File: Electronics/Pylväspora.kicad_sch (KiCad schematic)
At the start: 19 parts, among them SW1 SW_Push, SW2 SW_Push, U1 ATtiny814-SS, U2 AMS1117-3.3

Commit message: Corrected jst model footprints
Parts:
- Feedback1: footprint Connector_PinSocket_2.54mm:PinSocket_1x03_P2.54mm_Vertical -> Connector_JST:JST_EH_B3B-EH-A_1x03_P2.50mm_Vertical
- PWM_out1: footprint Connector_PinSocket_2.54mm:PinSocket_1x01_P2.54mm_Vertical -> Connector_PinHeader_2.54mm:PinHeader_1x01_P2.54mm_Vertical
- PWR1: footprint Connector_PinSocket_2.54mm:PinSocket_1x02_P2.54mm_Vertical -> Connector_JST:JST_EH_B2B-EH-A_1x02_P2.50mm_Vertical
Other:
- note added: "Buttons"
- note added: "Drill Press controller"
- note added: "Mounting"
- note added: "POWER"
- moved on the sheet: C1, C2, C3, C4, H2, H3, H4, PWR1, SW1, SW2, U2

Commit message: Software ios, display driving logic, buttons
Software ios, display driving logic, buttons
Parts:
- C1: value C -> 100u
- C2: value C -> 10u
- C3, C4: value C -> 10n
- R1, R2: value R -> 1k
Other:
- note added: "3.2mm Drillsize"
- note added: "Outputs"
- moved on the sheet: R1, pinheader1
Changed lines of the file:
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@@
+		)
+	)
+	(rectangle
+		(start 181.61 29.21)
+		(end 251.46 74.93)
+		(stroke
+			(width 0)
+			(type default)
+		)
+		(fill
+			(type none)
 		)
 	)
@@
 		)
 	)
+	(text "3.2mm Drillsize"
+		(exclude_from_sim no)
+		(at 68.834 127.254 0)
+		(effects
+			(font
+				(size 1.27 1.27)
+			)
+		)
+	)
+	(text "Outputs"
+		(exclude_from_sim no)
+		(at 225.298 34.036 0)
+		(effects
+			(font
+				(size 1.27 1.27)
+			)
+		)
+	)
 	(junction
 		(at 224.79 119.38)
@@
 	(wire
 		(pts
+			(xy 205.74 59.69) (xy 209.55 59.69)
+		)
+		(stroke
+			(width 0)
+			(type default)
+		)
+	)
+	(wire
+		(pts
 			(xy 224.79 119.38) (xy 224.79 124.46)
 		)
@@
 	(wire
 		(pts
-			(xy 198.12 62.23) (xy 209.55 62.23)
+			(xy 203.2 62.23) (xy 209.55 62.23)
 		)
 		(stroke
@@
 	(wire
 		(pts
+			(xy 205.74 55.88) (xy 205.74 59.69)
+		)
+		(stroke
+			(width 0)
+			(type default)
+		)
+	)
+	(wire
+		(pts
 			(xy 201.93 106.68) (xy 209.55 106.68)
 		)
@@
 	(wire
 		(pts
+			(xy 203.2 46.99) (xy 207.01 46.99)
+		)
+		(stroke
+			(width 0)
+			(type default)
+		)
+	)
+	(wire
+		(pts
+			(xy 203.2 46.99) (xy 203.2 48.26)
+		)
+		(stroke
+			(width 0)
+			(type default)
+		)
+	)
+	(wire
+		(pts
 			(xy 43.18 31.75) (xy 43.18 34.29)
 		)
@@
 	(wire
 		(pts
-			(xy 177.8 35.56) (xy 180.34 35.56)
+			(xy 204.47 39.37) (xy 207.01 39.37)
 		)
 		(stroke
@@
 	(wire
 		(pts
-			(xy 179.07 40.64) (xy 180.34 40.64)
-		)
-		(stroke
-			(width 0)
-			(type default)
-		)
-	)
-	(wire
-		(pts
-			(xy 177.8 38.1) (xy 180.34 38.1)
+			(xy 205.74 44.45) (xy 207.01 44.45)
+		)
+		(stroke
+			(width 0)
+			(type default)
+		)
+	)
+	(wire
+		(pts
+			(xy 204.47 41.91) (xy 207.01 41.91)
 		)
 		(stroke
@@
 	(wire
 		(pts
+			(xy 195.58 62.23) (xy 194.31 62.23)
+		)
+		(stroke
+			(width 0)
+			(type default)
+		)
+	)
+	(wire
+		(pts
 			(xy 107.95 78.74) (xy 111.76 78.74)
 		)
@@
 	(wire
 		(pts
-			(xy 204.47 59.69) (xy 209.55 59.69)
+			(xy 209.55 55.88) (xy 205.74 55.88)
 		)
 		(stroke
@@
 	(global_label "3.3V"
 		(shape input)
-		(at 204.47 59.69 180)
+		(at 209.55 55.88 180)
 		(fields_autoplaced yes)
 		(effects
@@
 		)
 		(property "Intersheetrefs" "${INTERSHEET_REFS}"
-			(at 197.3724 59.69 0)
+			(at 202.4524 55.88 0)
 			(effects
 				(font
@@
 	(global_label "3.3V"
 		(shape input)
-		(at 179.07 40.64 180)
+		(at 205.74 44.45 180)
 		(fields_autoplaced yes)
 		(effects
@@
 		)
 		(property "Intersheetrefs" "${INTERSHEET_REFS}"
-			(at 171.9724 40.64 0)
+			(at 198.6424 44.45 0)
 			(effects
 				(font
@@
 	(global_label "SCK"
 		(shape input)
-		(at 177.8 35.56 180)
+		(at 204.47 39.37 180)
 		(fields_autoplaced yes)
 		(effects
@@
 		)
 		(property "Intersheetrefs" "${INTERSHEET_REFS}"
-			(at 171.0653 35.56 0)
+			(at 197.7353 39.37 0)
 			(effects
 				(font
@@
 	(global_label "SDA"
 		(shape input)
-		(at 177.8 38.1 180)
+		(at 204.47 41.91 180)
 		(fields_autoplaced yes)
 		(effects
@@
 		)
 		(property "Intersheetrefs" "${INTERSHEET_REFS}"
-			(at 171.2467 38.1 0)
+			(at 197.9167 41.91 0)
 			(effects
 				(font
@@
 	(global_label "PA4"
 		(shape input)
-		(at 190.5 62.23 180)
+		(at 194.31 62.23 180)
 		(fields_autoplaced yes)
 		(effects
@@
 		)
 		(property "Intersheetrefs" "${INTERSHEET_REFS}"
-			(at 183.9467 62.23 0)
+			(at 187.7567 62.23 0)
 			(effects
 				(font
@@
 			)
 		)
-		(property "Value" "C"
+		(property "Value" "10u"
 			(at 78.74 46.9899 0)
 			(effects
@@
 			)
 		)
-		(property "Value" "R"
+		(property "Value" "1k"
 			(at 152.4 72.39 90)
 			(effects
@@
 			)
 		)
-		(property "Value" "C"
+		(property "Value" "10n"
 			(at 241.3 116.8399 0)
 			(effects
@@
 			)
 		)
-		(property "Value" "C"
+		(property "Value" "100u"
 			(at 50.8 46.9899 0)
 			(effects
@@
 	(symbol
 		(lib_id "power:GND")
-		(at 180.34 43.18 0)
+		(at 203.2 48.26 0)
 		(unit 1)
 		(exclude_from_sim no)
@@
 		(on_board yes)
 		(dnp no)
-		(fields_autoplaced yes)
 		(property "Reference" "#PWR05"
-			(at 180.34 49.53 0)
+			(at 203.2 54.61 0)
 			(effects
 				(font
@@
 		)
 		(property "Value" "GND"
-			(at 180.34 48.26 0)
+			(at 202.946 52.324 0)
 			(effects
 				(font
@@
 		)
 		(property "Footprint" ""
-			(at 180.34 43.18 0)
+			(at 203.2 48.26 0)
 			(effects
 				(font
@@
 		)
 		(property "Datasheet" ""
-			(at 180.34 43.18 0)
+			(at 203.2 48.26 0)
 			(effects
 				(font
@@
 		)
 		(property "Description" "Power symbol creates a global label with name \"GND\" , ground"
-			(at 180.34 43.18 0)
+			(at 203.2 48.26 0)
 			(effects
 				(font
@@
 	(symbol
 		(lib_id "Connector:Conn_01x04_Socket")
-		(at 185.42 38.1 0)
+		(at 212.09 41.91 0)
 		(unit 1)
 		(exclude_from_sim no)
@@
 		(fields_autoplaced yes)
 		(property "Reference" "pinheader1"
-			(at 186.69 38.0999 0)
+			(at 213.36 41.9099 0)
 			(effects
 				(font
@@
 		)
 		(property "Value" "Conn_01x04_Socket"
-			(at 186.69 40.6399 0)
+			(at 213.36 44.4499 0)
 			(effects
 				(font
@@
 		)
 		(property "Footprint" "Connector_PinSocket_2.54mm:PinSocket_1x04_P2.54mm_Vertical"
-			(at 185.42 38.1 0)
+			(at 212.09 41.91 0)
 			(effects
 				(font
@@
 		)
 		(property "Datasheet" "~"
-			(at 185.42 38.1 0)
+			(at 212.09 41.91 0)
 			(effects
 				(font
@@
 		)
 		(property "Description" "Generic connector, single row, 01x04, script generated"
-			(at 185.42 38.1 0)
+			(at 212.09 41.91 0)
 			(effects
 				(font
@@
 	(symbol
 		(lib_id "Device:R")
-		(at 194.31 62.23 90)
+		(at 199.39 62.23 90)
 		(unit 1)
 		(exclude_from_sim no)
@@
 		(fields_autoplaced yes)
 		(property "Reference" "R1"
-			(at 194.31 55.88 90)
-			(effects
-				(font
-					(size 1.27 1.27)
-				)
-			)
-		)
-		(property "Value" "R"
-			(at 194.31 58.42 90)
+			(at 199.39 55.88 90)
+			(effects
+				(font
+					(size 1.27 1.27)
+				)
+			)
+		)
+		(property "Value" "1k"
+			(at 199.39 58.42 90)
 			(effects
 				(font
@@
 		)
 		(property "Footprint" "Resistor_SMD:R_1206_3216Metric_Pad1.30x1.75mm_HandSolder"
-			(at 194.31 64.008 90)
+			(at 199.39 64.008 90)
 			(effects
 				(font
@@
 		)
 		(property "Datasheet" "~"
-			(at 194.31 62.23 0)
+			(at 199.39 62.23 0)
 			(effects
 				(font
@@
 		)
 		(property "Description" "Resistor"
-			(at 194.31 62.23 0)
+			(at 199.39 62.23 0)
 			(effects
 				(font
@@
 			)
 		)
-		(property "Value" "C"
-			(at 197.612 117.348 0)
-			(effects
-				(font
+		(property "Value" "10n"
+			(at 195.58 117.094 0)
+			(effects
+				(font

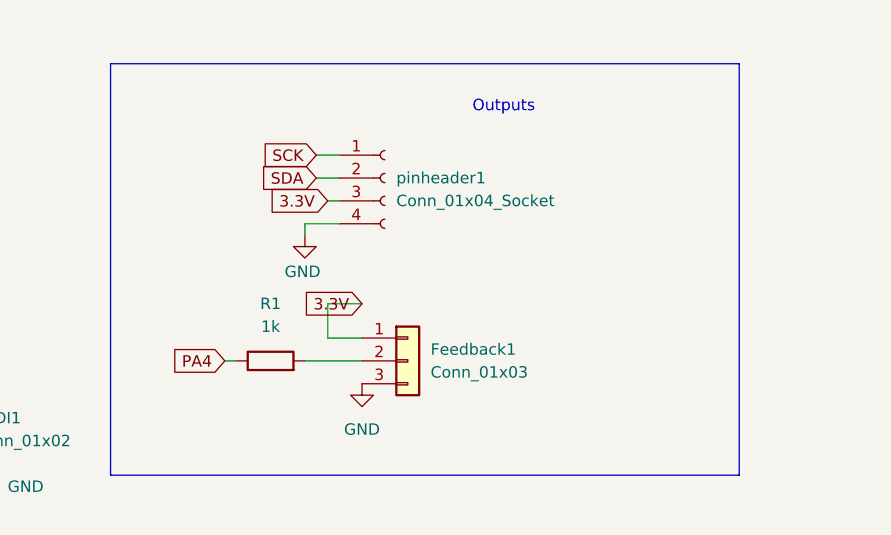
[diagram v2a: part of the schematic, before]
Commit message: Small schematic and layout fix
Forgot a pullup resistor from hall input, added 4.7k pullup. Fixed incorrect measurement of RPM and increased update frequency in software
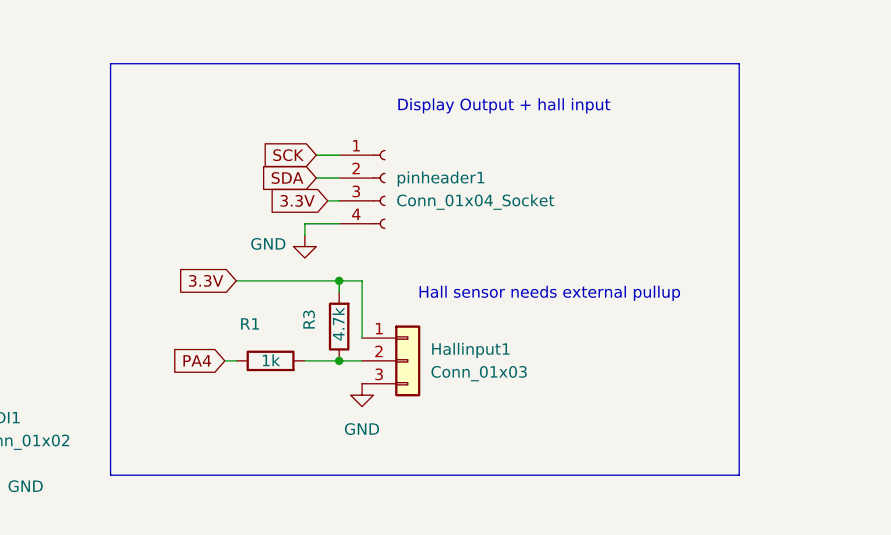
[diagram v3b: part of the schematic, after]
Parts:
- added R3: 4.7k, Resistor_SMD:R_1206_3216Metric_Pad1.30x1.75mm_HandSolder, symbol Device:R
- renumbered Feedback1 to Hallinput1
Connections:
- net 3.3V: now also R3.2
- net at Hallinput1.2 (Pin_2), R1.2: now also R3.1
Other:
- note added: "Display Output + hall input"
- note added: "Hall sensor needs external pullup"
- note removed: "Outputs"
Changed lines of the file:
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@@
+		)
+	)
+	(text "Hall sensor needs external pullup"
+		(exclude_from_sim no)
+		(at 230.378 54.864 0)
+		(effects
+			(font
+				(size 1.27 1.27)
+			)
 		)
 	)
@@
 		)
 	)
-	(text "Outputs"
+	(text "Display Output + hall input"
 		(exclude_from_sim no)
 		(at 225.298 34.036 0)
@@
 	)
 	(junction
+		(at 207.01 53.34)
+		(diameter 0)
+		(color 0 0 0 0)
+	)
+	(junction
+		(at 207.01 62.23)
+		(diameter 0)
+		(color 0 0 0 0)
+	)
+	(junction
 		(at 43.18 34.29)
 		(diameter 0)
@@
 	(wire
 		(pts
-			(xy 205.74 59.69) (xy 209.55 59.69)
-		)
-		(stroke
-			(width 0)
-			(type default)
-		)
-	)
-	(wire
-		(pts
 			(xy 224.79 119.38) (xy 224.79 124.46)
 		)
@@
 	(wire
 		(pts
-			(xy 203.2 62.23) (xy 209.55 62.23)
+			(xy 203.2 62.23) (xy 207.01 62.23)
 		)
 		(stroke
@@
 	(wire
 		(pts
-			(xy 205.74 55.88) (xy 205.74 59.69)
-		)
-		(stroke
-			(width 0)
-			(type default)
-		)
-	)
-	(wire
-		(pts
 			(xy 201.93 106.68) (xy 209.55 106.68)
 		)
@@
 	(wire
 		(pts
+			(xy 207.01 53.34) (xy 207.01 54.61)
+		)
+		(stroke
+			(width 0)
+			(type default)
+		)
+	)
+	(wire
+		(pts
 			(xy 38.1 34.29) (xy 43.18 34.29)
 		)
@@
 	(wire
 		(pts
+			(xy 207.01 53.34) (xy 209.55 53.34)
+		)
+		(stroke
+			(width 0)
+			(type default)
+		)
+	)
+	(wire
+		(pts
 			(xy 149.86 81.28) (xy 146.05 81.28)
 		)
@@
 	(wire
 		(pts
+			(xy 209.55 53.34) (xy 209.55 59.69)
+		)
+		(stroke
+			(width 0)
+			(type default)
+		)
+	)
+	(wire
+		(pts
 			(xy 195.58 62.23) (xy 194.31 62.23)
 		)
@@
 	(wire
 		(pts
-			(xy 209.55 55.88) (xy 205.74 55.88)
+			(xy 195.58 53.34) (xy 207.01 53.34)
 		)
 		(stroke
@@
 		(pts
 			(xy 237.49 111.76) (xy 237.49 107.95)
+		)
+		(stroke
+			(width 0)
+			(type default)
+		)
+	)
+	(wire
+		(pts
+			(xy 207.01 62.23) (xy 209.55 62.23)
 		)
 		(stroke
@@
 	(global_label "3.3V"
 		(shape input)
-		(at 209.55 55.88 180)
+		(at 195.58 53.34 180)
 		(fields_autoplaced yes)
 		(effects
@@
 		)
 		(property "Intersheetrefs" "${INTERSHEET_REFS}"
-			(at 202.4524 55.88 0)
+			(at 188.4824 53.34 0)
 			(effects
 				(font
@@
 	)
 	(symbol
+		(lib_id "Device:R")
+		(at 207.01 58.42 180)
+		(unit 1)
+		(exclude_from_sim no)
+		(in_bom yes)
+		(on_board yes)
+		(dnp no)
+		(property "Reference" "R3"
+			(at 203.708 57.658 90)
+			(effects
+				(font
+					(size 1.27 1.27)
+				)
+			)
+		)
+		(property "Value" "4.7k"
+			(at 207.01 58.166 90)
+			(effects
+				(font
+					(size 1.27 1.27)
+				)
+			)
+		)
+		(property "Footprint" "Resistor_SMD:R_1206_3216Metric_Pad1.30x1.75mm_HandSolder"
+			(at 208.788 58.42 90)
+			(effects
+				(font
+					(size 1.27 1.27)
+				)
+				(hide yes)
+			)
+		)
+		(property "Datasheet" "~"
+			(at 207.01 58.42 0)
+			(effects
+				(font
+					(size 1.27 1.27)
+				)
+				(hide yes)
+			)
+		)
+		(property "Description" "Resistor"
+			(at 207.01 58.42 0)
+			(effects
+				(font
+					(size 1.27 1.27)
+				)
+				(hide yes)
+			)
+		)
+		(pin "1"
+		)
+		(pin "2"
+		)
+		(instances
+			(project "Pylväspora"
+				(path "/20710b63-7e35-457a-8d30-c30f218c011d"
+					(reference "R3")
+					(unit 1)
+				)
+			)
+		)
+	)
+	(symbol
 		(lib_id "Connector_Generic:Conn_01x02")
 		(at 33.02 36.83 180)
@@
 		)
 		(property "Value" "GND"
-			(at 202.946 52.324 0)
+			(at 199.136 49.276 0)
 			(effects
 				(font
@@
 		(dnp no)
 		(fields_autoplaced yes)
-		(property "Reference" "Feedback1"
+		(property "Reference" "Hallinput1"
 			(at 217.17 60.9599 0)
 			(effects
@@
 			(project ""
 				(path "/20710b63-7e35-457a-8d30-c30f218c011d"
-					(reference "Feedback1")
+					(reference "Hallinput1")
 					(unit 1)
 				)
@@
 		(on_board yes)
 		(dnp no)
-		(fields_autoplaced yes)
 		(property "Reference" "R1"
-			(at 199.39 55.88 90)
+			(at 197.104 58.166 90)
 			(effects
 				(font
@@
 		)
 		(property "Value" "1k"
-			(at 199.39 58.42 90)
-			(effects
-				(font
+			(at 199.39 62.23 90)
+			(effects
+				(font
